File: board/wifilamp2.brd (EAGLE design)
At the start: 45.1 x 28.6 mm, 5 parts

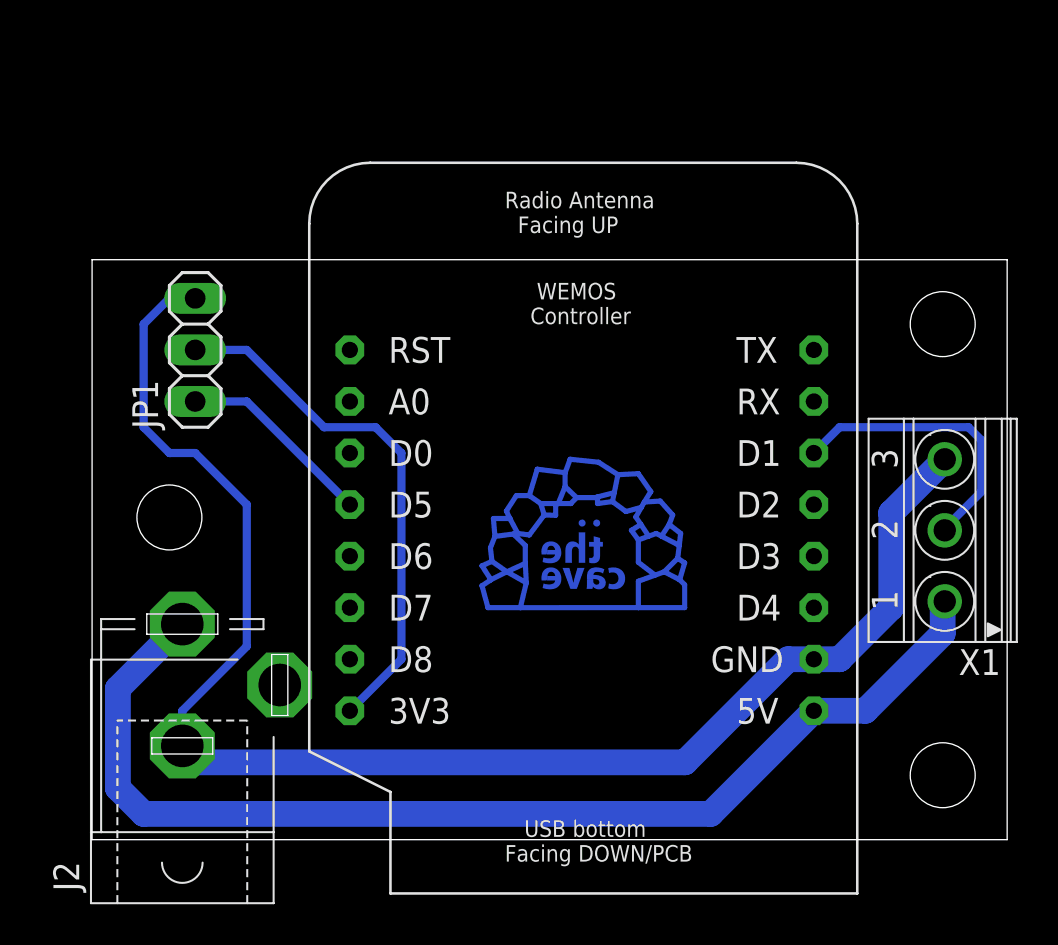
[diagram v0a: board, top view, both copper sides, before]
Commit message: [Board] update board files to rev 2
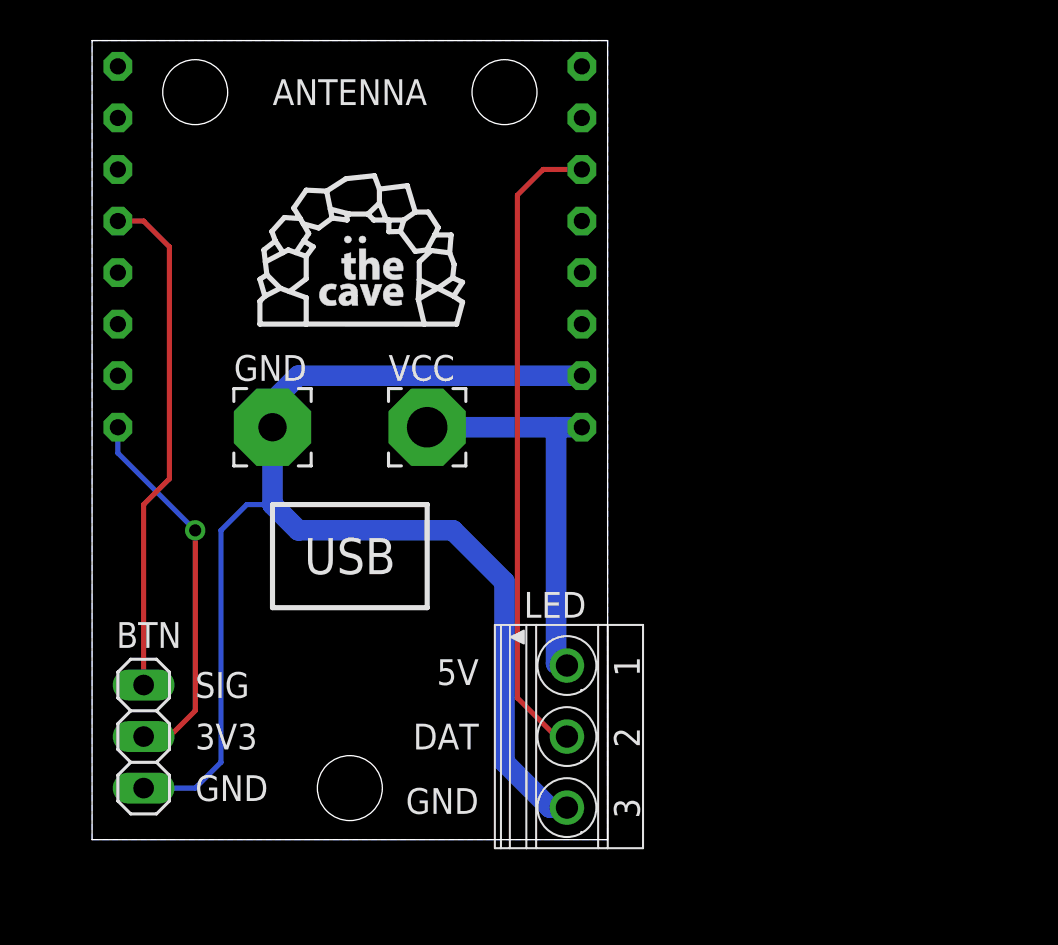
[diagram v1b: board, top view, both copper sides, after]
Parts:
- removed J2: (no value), con-jack-pc-gk21:PC-GK21
- removed JP1: (no value), pinhead:1X03
- removed X1: (no value), con-phoenix-350:1751251
- added BTN: (no value), pinhead:1X03
- added GND: (no value), wirepad:3,81/1,4
- added LED: (no value), con-phoenix-350:1751251
- added VCC: (no value), thecave:PAD3,81/2
- U$1: value WEMOS -> WEMOSPLAIN; device d1-mini:WEMOS -> d1-mini:WEMOS-PLAIN
- U$2: value THECAVE_LOGO_COPPER_SMALL -> THECAVE_LOGO_TOP_SMALL; device thecave:COPPER_SMALL -> thecave:LOGO_TOP_SMALL
- moved U$2 25.2 mm to (8.26, 25.4), flipped to the top
- moved U$1 18.1 mm to (1.27, 20.3)
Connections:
- net +3V3: now also BTN.2; no longer JP1.2
- net +5V: now also LED.1, VCC.1; no longer J2.3, X1.1
- net GND: now also BTN.3, GND.1, LED.3; no longer J2.1, JP1.3, X1.3
- net N$2: now also LED.2; no longer X1.2
- net TOUCH: now also BTN.1; no longer JP1.1
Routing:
- net +5V: track 55.9 -> 19.8 mm
- net N$2: track 14.2 -> 31.7 mm
- net TOUCH: track 9.72 -> 25.2 mm
- net GND: track 74.8 -> 65.6 mm
- net +3V3: track 26.0 -> 18.6 mm, vias 0 -> 1
- added copper zone on layer 16, net GND
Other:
- board size 45.1 x 28.6 mm -> 25.4 x 39.4 mm
- board text added: "3V3"
- board text added: "5V"
- board text added: "ANTENNA"
- board text added: "DAT"
- board text added: "GND"
- board text added: "SIG"
- board text added: "USB"
